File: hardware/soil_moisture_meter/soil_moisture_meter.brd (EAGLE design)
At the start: 149.9 x 33 mm, 16 parts, among them IC1 MEGA328, IC2 RFM12, IC3 74HC14D

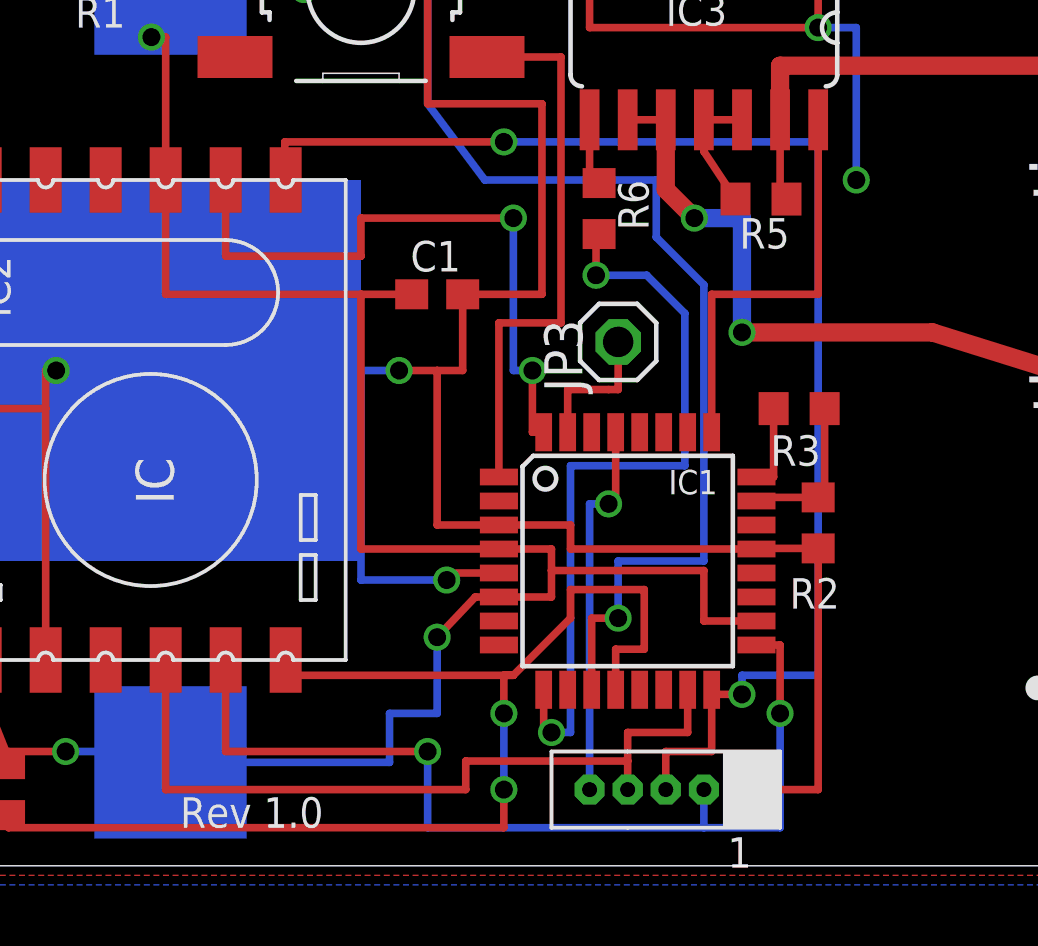
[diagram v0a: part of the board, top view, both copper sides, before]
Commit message: Remove battery measurement resistors.
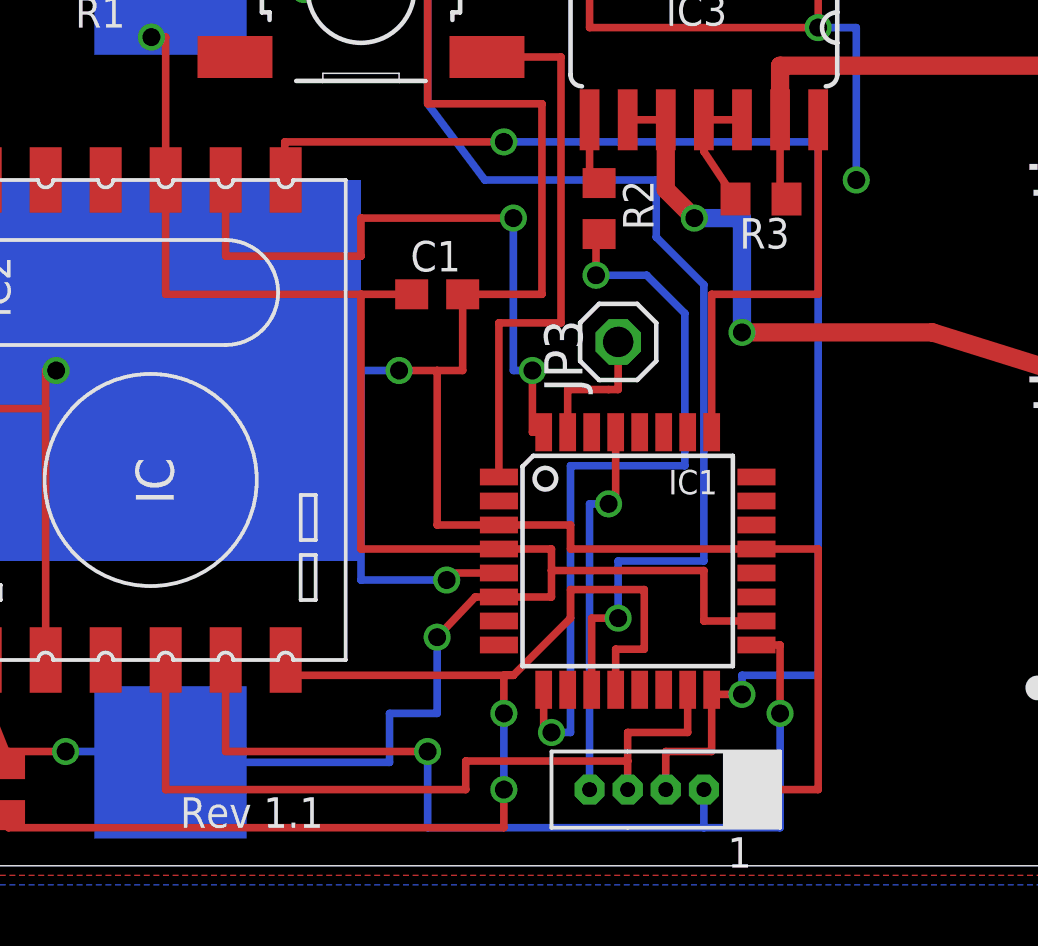
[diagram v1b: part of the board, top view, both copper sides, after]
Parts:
- removed R5: 100k, rcl:R0603
- removed R6: 220R, rcl:R0603
- R2: value 47k -> 220R
- moved R2 12.8 mm to (24.4, 21.9), turned to 270 degrees
- moved R3 7.10 mm to (29.8, 22.2)
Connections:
- removed net N$1: IC1.24, R3.2
- removed net N$14: IC1.23, R2.2, R3.1
- net GND: no longer R2.1
- net N$10: now also R2.1; no longer R6.1
- net N$11: now also R2.2; no longer R6.2
- net N$2: now also R3.2; no longer R5.2
- net N$9: now also R3.1; no longer R5.1
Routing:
- net N$14: track 5.35 -> 0.00 mm
- net N$1: track 2.85 -> 0.00 mm
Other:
- board text added: "Rev 1.1"
- board text removed: "Rev 1.0"
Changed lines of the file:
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@@
 <setting verticaltext="up"/>
 </settings>
-<grid distance="0.05" unitdist="inch" unit="inch" style="lines" multiple="1" display="yes" altdistance="0.0125" altunitdist="inch" altunit="inch"/>
+<grid distance="0.05" unitdist="inch" unit="inch" style="lines" multiple="1" display="yes" altdistance="0.000000123031" altunitdist="inch" altunit="inch"/>
 <layers>
 <layer number="1" name="Top" color="4" fill="1" visible="yes" active="yes"/>
@@
 <text x="40.64" y="9.525" size="1.778" layer="25" font="vector" rot="R90">smarthomatic</text>
 <text x="43.18" y="9.525" size="1.27" layer="25" font="vector" rot="R90">Soil Moisture Meter</text>
-<text x="10.4775" y="1.27" size="1.016" layer="25">Rev 1.0</text>
+<text x="10.4775" y="1.27" size="1.016" layer="25">Rev 1.1</text>
 <rectangle x1="43.270203125" y1="3.9345125" x2="43.351203125" y2="3.94029375" layer="25" rot="R90"/>
 <rectangle x1="41.365403125" y1="5.9261125" x2="45.256003125" y2="5.93189375" layer="25" rot="R90"/>
@@
 <attribute name="NAME" x="26.67" y="28.0035" size="1.016" layer="25" ratio="10"/>
 </element>
-<element name="R2" library="rcl" package="R0603" value="47k" x="31.75" y="11.43" smashed="yes" rot="R90">
-<attribute name="NAME" x="30.7975" y="8.5725" size="1.016" layer="25"/>
-<attribute name="VALUE" x="33.655" y="10.16" size="1.016" layer="27" rot="R90"/>
-</element>
-<element name="R3" library="rcl" package="R0603" value="100k" x="31.115" y="15.24" smashed="yes" rot="R180">
-<attribute name="NAME" x="30.1625" y="13.335" size="1.016" layer="25"/>
-<attribute name="VALUE" x="29.845" y="16.1925" size="1.016" layer="27"/>
-</element>
 <element name="R1" library="rcl" package="R0603" value="220R" x="7.9375" y="29.845" smashed="yes" rot="R180">
 <attribute name="NAME" x="6.985" y="27.94" size="1.016" layer="25"/>
@@
 <attribute name="VALUE" x="6.6675" y="1.27" size="1.016" layer="27" rot="R90"/>
 </element>
-<element name="R5" library="rcl" package="R0603" value="100k" x="29.845" y="22.225" smashed="yes" rot="R180">
+<element name="R3" library="rcl" package="R0603" value="100k" x="29.845" y="22.225" smashed="yes" rot="R180">
 <attribute name="NAME" x="30.7975" y="21.59" size="1.016" layer="25" rot="R180"/>
 <attribute name="VALUE" x="28.2575" y="19.3675" size="1.016" layer="27"/>
 </element>
-<element name="R6" library="rcl" package="R0603" value="220R" x="24.4475" y="21.9075" smashed="yes" rot="R270">
-<attribute name="NAME" x="25.0825" y="22.86" size="1.016" layer="25" rot="R270"/>
-<attribute name="VALUE" x="23.8125" y="20.0025" size="1.016" layer="27" rot="R90"/>
+<element name="R2" library="rcl" package="R0603" value="220R" x="24.4475" y="21.9075" smashed="yes" rot="R270">
+<attribute name="NAME" x="25.24595" y="22.86" size="1.016" layer="25" rot="R270"/>
+<attribute name="VALUE" x="23.64905" y="20.04341875" size="1.016" layer="27" rot="R90"/>
 </element>
 <element name="C1" library="resistor" package="C0603" value="1µF" x="19.05" y="19.05" smashed="yes">
@@
 <contactref element="JP1" pad="GND"/>
 <contactref element="LED1" pad="K"/>
-<contactref element="R2" pad="1"/>
 <contactref element="IC3" pad="1"/>
 <contactref element="IC3" pad="7"/>
@@
 <wire x1="23.495" y1="10.56" x2="29.6926" y2="10.56" width="0.254" layer="1"/>
 <wire x1="29.6926" y1="10.56" x2="29.6926" y2="10.58" width="0.254" layer="1"/>
-<wire x1="29.6926" y1="10.58" x2="31.75" y2="10.58" width="0.254" layer="1"/>
 <wire x1="29.21" y1="2.54" x2="31.75" y2="2.54" width="0.254" layer="1"/>
-<wire x1="31.75" y1="2.54" x2="31.75" y2="10.58" width="0.254" layer="1"/>
 <wire x1="24.13" y1="31.0134" x2="24.13" y2="27.94" width="0.254" layer="1"/>
 <wire x1="24.13" y1="27.94" x2="31.75" y2="27.94" width="0.254" layer="1"/>
@@
 <wire x1="31.75" y1="27.94" x2="33.02" y2="27.94" width="0.254" layer="16"/>
 <wire x1="33.02" y1="27.94" x2="33.02" y2="22.86" width="0.254" layer="16"/>
+<wire x1="29.6926" y1="10.56" x2="31.75" y2="10.56" width="0.254" layer="1"/>
+<wire x1="31.75" y1="10.56" x2="31.75" y2="2.54" width="0.254" layer="1"/>
 </signal>
 <signal name="VCC">
@@
 <wire x1="18.7325" y1="25.4" x2="18.7325" y2="29.21" width="0.254" layer="16"/>
 </signal>
-<signal name="N$14">
-<contactref element="IC1" pad="23"/>
-<contactref element="R2" pad="2"/>
-<contactref element="R3" pad="1"/>
-<wire x1="29.6926" y1="12.16" x2="29.6926" y2="12.28" width="0.254" layer="1"/>
-<wire x1="29.6926" y1="12.28" x2="31.75" y2="12.28" width="0.254" layer="1"/>
-<wire x1="31.75" y1="12.28" x2="31.965" y2="12.28" width="0.254" layer="1"/>
-<wire x1="31.965" y1="12.28" x2="31.965" y2="15.24" width="0.254" layer="1"/>
-</signal>
 <signal name="N$16">
 <contactref element="IC2" pad="8"/>
@@
 <wire x1="1.905" y1="5.9075" x2="2" y2="6.86" width="0.4064" layer="1"/>
 </signal>
-<signal name="N$1">
-<contactref element="IC1" pad="24"/>
-<contactref element="R3" pad="2"/>
-<wire x1="30.265" y1="15.24" x2="30.265" y2="12.96" width="0.254" layer="1"/>
-<wire x1="30.265" y1="12.96" x2="29.6926" y2="12.96" width="0.254" layer="1"/>
-</signal>
 <signal name="N$2">
 <contactref element="IC3" pad="12"/>
 <contactref element="IC3" pad="11"/>
-<contactref element="R5" pad="2"/>
+<contactref element="R3" pad="2"/>
 <wire x1="27.94" y1="24.8666" x2="27.94" y2="23.8125" width="0.254" layer="1"/>
 <wire x1="27.94" y1="23.8125" x2="28.995" y2="22.225" width="0.254" layer="1"/>
@@
 <signal name="N$9">
 <contactref element="IC3" pad="13"/>
-<contactref element="R5" pad="1"/>
+<contactref element="R3" pad="1"/>
 <wire x1="30.48" y1="24.8666" x2="30.48" y2="22.225" width="0.254" layer="1"/>
 <wire x1="30.48" y1="22.225" x2="30.695" y2="22.225" width="0.254" layer="1"/>
@@
 <signal name="N$10">
 <contactref element="IC3" pad="8"/>
-<contactref element="R6" pad="1"/>
+<contactref element="R2" pad="1"/>
 <wire x1="24.4475" y1="22.7575" x2="24.2325" y2="22.86" width="0.254" layer="1"/>
 <wire x1="24.13" y1="24.8666" x2="24.13" y2="22.7575" width="0.254" layer="1"/>
@@
 <signal name="N$11">
 <contactref element="IC1" pad="9"/>
-<contactref element="R6" pad="2"/>
+<contactref element="R2" pad="2"/>
 <wire x1="22.6" y1="5.8674" x2="22.6" y2="4.445" width="0.254" layer="1"/>
 <wire x1="22.6" y1="4.445" x2="22.86" y2="4.445" width="0.254" layer="1"/>

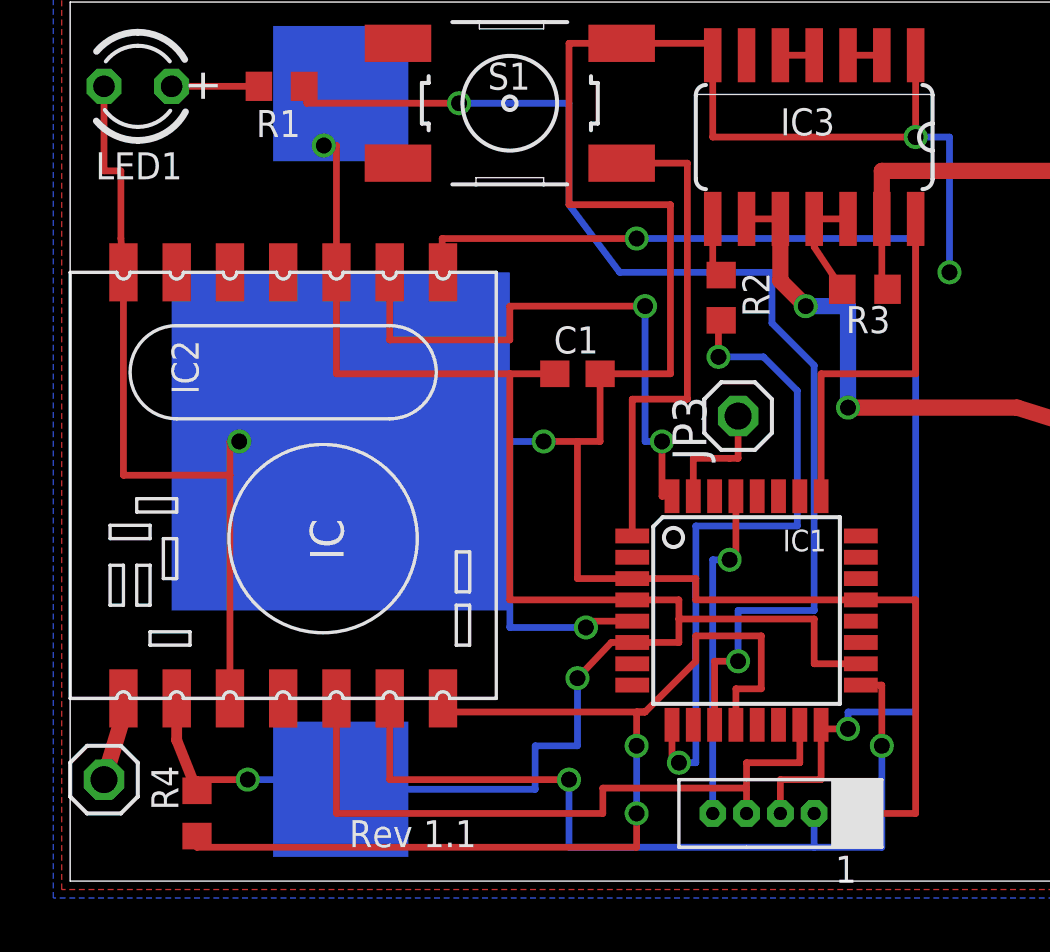
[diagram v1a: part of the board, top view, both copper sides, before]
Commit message: Change mini ISP connector and add 6th pin for VCC. Add solder jumper for VCC. Move ANT pin near RFM12B module. Remove resistor between 74GC14D and ATMega. Change LED resistor value.
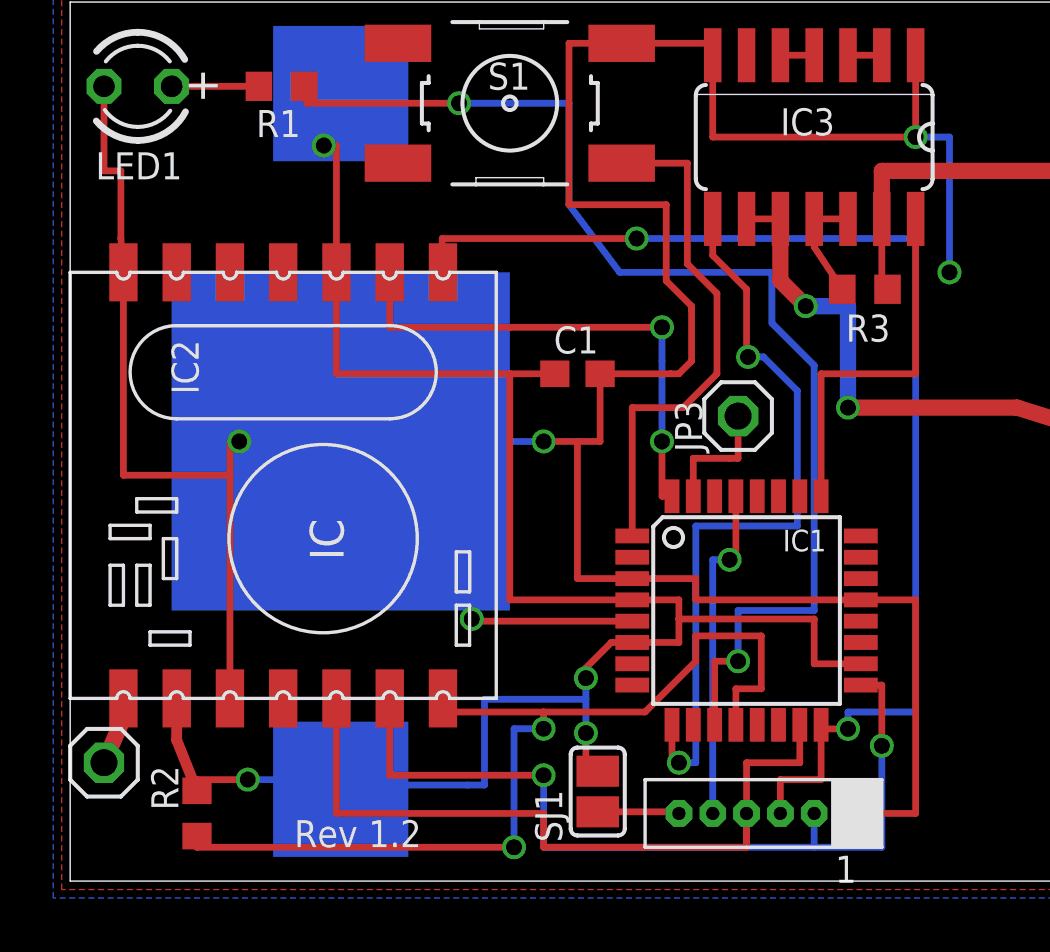
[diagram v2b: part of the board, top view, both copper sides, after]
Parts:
- removed R4: 1M, rcl:R0603
- added SJ1: VCC, jumper:SJ
- JP1: device shc_mini_isp:PINHD_1X5_1.27 -> shc_mini_isp:PINHD_1X6_1.27
- R1: value 220R -> 560R
- R2: value 220R -> 1M
- moved R2 27.6 mm to (4.76, 2.54), turned to 90 degrees
- moved JP2 0.64 mm to (1.27, 4.45)
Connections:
- removed net N$11: IC1.9, R2.2
- new net N$1: JP1.VCC, SJ1.2
- net N$10: now also IC1.9; no longer R2.1
- net N$13: now also R2.1; no longer R4.1
- net VCC: now also R2.2, SJ1.1; no longer R4.2
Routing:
- net N$10: track 2.66 -> 28.2 mm, vias 0 -> 2
- net N$11: track 25.1 -> 0.00 mm, vias 2 -> 0
- net VCC: track 74.0 -> 77.9 mm, vias 3 -> 4
- net N$13: track 40.8 -> 37.0 mm
- net GND: track 131.2 -> 134.3 mm
- net N$1: track 0.00 -> 3.07 mm
- net N$3: track 26.0 -> 28.8 mm
- net N$15: track 21.5 -> 19.0 mm
- net N$19: track 18.5 -> 19.4 mm
- net N$16: track 3.15 -> 2.55 mm
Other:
- board text added: "GND"
- board text added: "Rev 1.2"
- board text removed: "Rev 1.1"
